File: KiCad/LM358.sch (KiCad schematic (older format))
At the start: 13 parts, among them IC1 LM358

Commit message: correção P1: LCD e Capacitores
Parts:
- added CS4: C, Capacitor_SMD:C_0805_2012Metric_Pad1.18x1.45mm_HandSolder, symbol Device:C
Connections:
- net GNDREF: now also CS4.1
- net Vcc_5v: now also CS4.2
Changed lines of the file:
@@
 $EndComp
 Wire Wire Line
-	5950 3000 6100 3000
+	5950 3000 6050 3000
 Text HLabel 6150 3600 2    50   BiDi ~ 0
 V+_2
@@
 Text Notes 5100 2600 0    50   ~ 0
 Saturação 0,3v-3,3v
+$Comp
+L power:GNDREF #PWR?
+U 1 1 60FB68FD
+P 6900 2650
+AR Path="/60FB68FD" Ref="#PWR?"  Part="1"
+AR Path="/60B29ED3/60FB68FD" Ref="#PWR05"  Part="1"
+F 0 "#PWR05" H 6900 2400 50  0001 C CNN
+F 1 "GNDREF" H 6905 2477 50  0000 C CNN
+F 2 "" H 6900 2650 50  0001 C CNN
+F 3 "" H 6900 2650 50  0001 C CNN
+	1    6900 2650
+	1    0    0    -1
+$EndComp
+$Comp
+L Device:C CS?
+U 1 1 60FB6903
+P 6700 2550
+AR Path="/60FB6903" Ref="CS?"  Part="1"
+AR Path="/60B29ED3/60FB6903" Ref="CS4"  Part="1"
+F 0 "CS4" V 6448 2550 50  0000 C CNN
+F 1 "C" V 6539 2550 50  0000 C CNN
+F 2 "Capacitor_SMD:C_0805_2012Metric_Pad1.18x1.45mm_HandSolder" H 6738 2400 50  0001 C CNN
+F 3 "~" H 6700 2550 50  0001 C CNN
+	1    6700 2550
+	0    1    1    0
+$EndComp
+Wire Wire Line
+	6900 2650 6900 2550
+Wire Wire Line
+	6900 2550 6850 2550
+Wire Wire Line
+	6550 2550 6050 2550
+Wire Wire Line
+	6050 2550 6050 3000
+Connection ~ 6050 3000
+Wire Wire Line
+	6050 3000 6100 3000
 $EndSCHEMATC

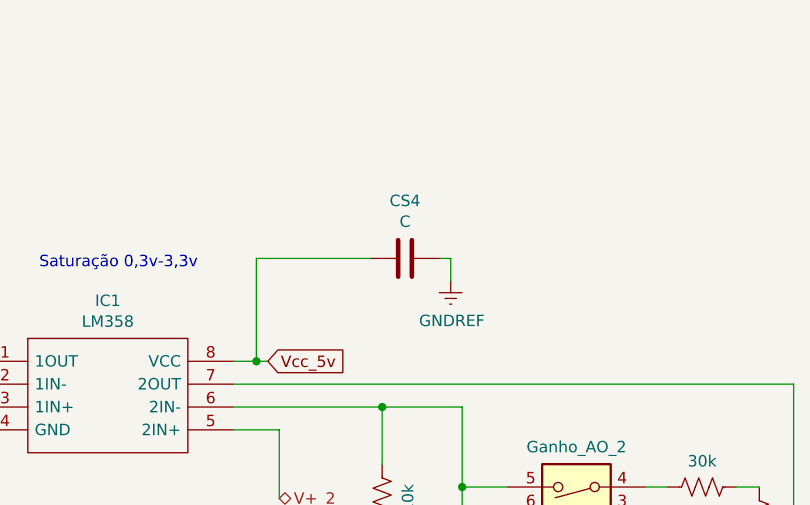
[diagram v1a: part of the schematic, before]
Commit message: Valores dos capacitores CS
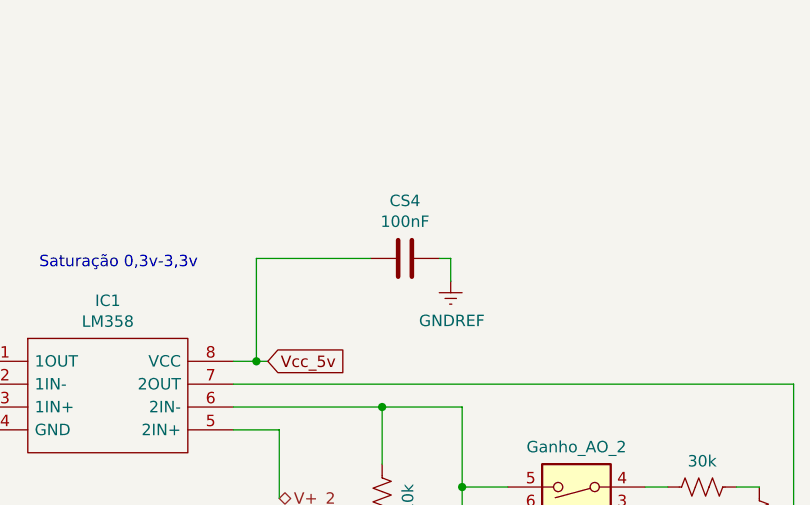
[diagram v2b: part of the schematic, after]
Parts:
- CS4: value C -> 100nF
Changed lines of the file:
@@
 AR Path="/60B29ED3/60FB6903" Ref="CS4"  Part="1"
 F 0 "CS4" V 6448 2550 50  0000 C CNN
-F 1 "C" V 6539 2550 50  0000 C CNN
+F 1 "100nF" V 6539 2550 50  0000 C CNN
 F 2 "Capacitor_SMD:C_0805_2012Metric_Pad1.18x1.45mm_HandSolder" H 6738 2400 50  0001 C CNN
 F 3 "~" H 6700 2550 50  0001 C CNN
